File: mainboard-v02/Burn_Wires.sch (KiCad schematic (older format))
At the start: 41 parts, among them Q2 2N5088, Q3 2N5088, Q4 IRLML2803, Q5 IRLML2803, Q6 IRLML2803, Q7 IRLML2803, Q8 IRLML2803, U16 PE014006, U17 PE014006, U18 NDS8434, U19 NDS8434, U20 NDS8434, U21 NDS8434, U22 NDS8434

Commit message: fixing bold font and adding schematic pdf of v02
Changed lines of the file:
@@
 EESchema Schematic File Version 4
-LIBS:mainboard
 EELAYER 29 0
 EELAYER END
@@
 	6000 1700 6300 1700
 Connection ~ 6000 1700
-Text GLabel 6000 1700 0    10   BiDi ~ 0
+Text GLabel 6000 1700 0    10   BiDi ~ 2
 GND
 Wire Wire Line
@@
 	6000 2650 6000 2750
 Connection ~ 6000 2650
-Text GLabel 6300 2650 0    10   BiDi ~ 0
+Text GLabel 6300 2650 0    10   BiDi ~ 2
 GND
 Wire Wire Line
 	6400 4300 6100 4300
 Connection ~ 6100 4300
-Text GLabel 6400 4300 0    10   BiDi ~ 0
+Text GLabel 6400 4300 0    10   BiDi ~ 2
 GND
 Wire Wire Line
 	6100 5150 6400 5150
 Connection ~ 6100 5150
-Text GLabel 6100 5150 0    10   BiDi ~ 0
+Text GLabel 6100 5150 0    10   BiDi ~ 2
 GND
 Wire Wire Line
 	6100 6000 6400 6000
 Connection ~ 6100 6000
-Text GLabel 6100 6000 0    10   BiDi ~ 0
+Text GLabel 6100 6000 0    10   BiDi ~ 2
 GND
 Wire Wire Line
 	8600 2350 8900 2350
-Text GLabel 8600 2350 0    10   BiDi ~ 0
+Text GLabel 8600 2350 0    10   BiDi ~ 2
 GND
 Wire Wire Line
 	8700 4000 9000 4000
-Text GLabel 8700 4000 0    10   BiDi ~ 0
+Text GLabel 8700 4000 0    10   BiDi ~ 2
 GND
 Wire Wire Line
@@
 Wire Wire Line
 	5400 7400 5400 7500
-Text GLabel 5300 7400 0    10   BiDi ~ 0
+Text GLabel 5300 7400 0    10   BiDi ~ 2
 GND
 Wire Wire Line
@@
 Wire Wire Line
 	2000 7400 1900 7400
-Text GLabel 2000 7500 0    10   BiDi ~ 0
+Text GLabel 2000 7500 0    10   BiDi ~ 2
 GND
 Wire Wire Line
@@
 Wire Wire Line
 	3600 7400 3600 7500
-Text GLabel 3500 7400 0    10   BiDi ~ 0
+Text GLabel 3500 7400 0    10   BiDi ~ 2
 GND
 Wire Wire Line
 	8600 1400 8900 1400
-Text GLabel 8600 1400 0    10   BiDi ~ 0
+Text GLabel 8600 1400 0    10   BiDi ~ 2
 GND
 Wire Wire Line
 	8700 4850 9000 4850
-Text GLabel 8700 4850 0    10   BiDi ~ 0
+Text GLabel 8700 4850 0    10   BiDi ~ 2
 GND
 Wire Wire Line
 	8700 5700 9000 5700
-Text GLabel 8700 5700 0    10   BiDi ~ 0
+Text GLabel 8700 5700 0    10   BiDi ~ 2
 GND
 Wire Wire Line
@@
 	2000 2100 2300 2100
 Connection ~ 2300 2100
-Text GLabel 2300 2200 0    10   BiDi ~ 0
+Text GLabel 2300 2200 0    10   BiDi ~ 2
 GND
 Wire Wire Line
@@
 	2400 4500 2400 4700
 Connection ~ 2400 4700
-Text GLabel 2100 4700 0    10   BiDi ~ 0
+Text GLabel 2100 4700 0    10   BiDi ~ 2
 GND
 Text Label 8500 4000 2    50   ~ 0
@@
 	0    -1   -1   0
 $EndComp
-Text Notes 2700 1900 0    85   ~ 0
+Text Notes 2700 1900 0    85   ~ 17
 Power Relay A
-Text Notes 4500 800  0    85   ~ 0
+Text Notes 4500 800  0    85   ~ 17
 Burn Wire Control (Antenna Depolyment)
-Text Notes 4500 3300 0    85   ~ 0
+Text Notes 4500 3300 0    85   ~ 17
 Burn Wire Control (Sprite deployment)
-Text Notes 2800 4600 0    85   ~ 0
+Text Notes 2800 4600 0    85   ~ 17
 Power Relay B
-Text Notes 8200 1150 0    85   ~ 0
+Text Notes 8200 1150 0    85   ~ 17
 Antenna Board\nConnectors
-Text Notes 8300 3800 0    85   ~ 0
+Text Notes 8300 3800 0    85   ~ 17
 Solar Panel Board\nConnectors
-Text Notes 3000 6700 0    85   ~ 0
+Text Notes 3000 6700 0    85   ~ 17
 Solar Panel Connectors
 Wire Wire Line

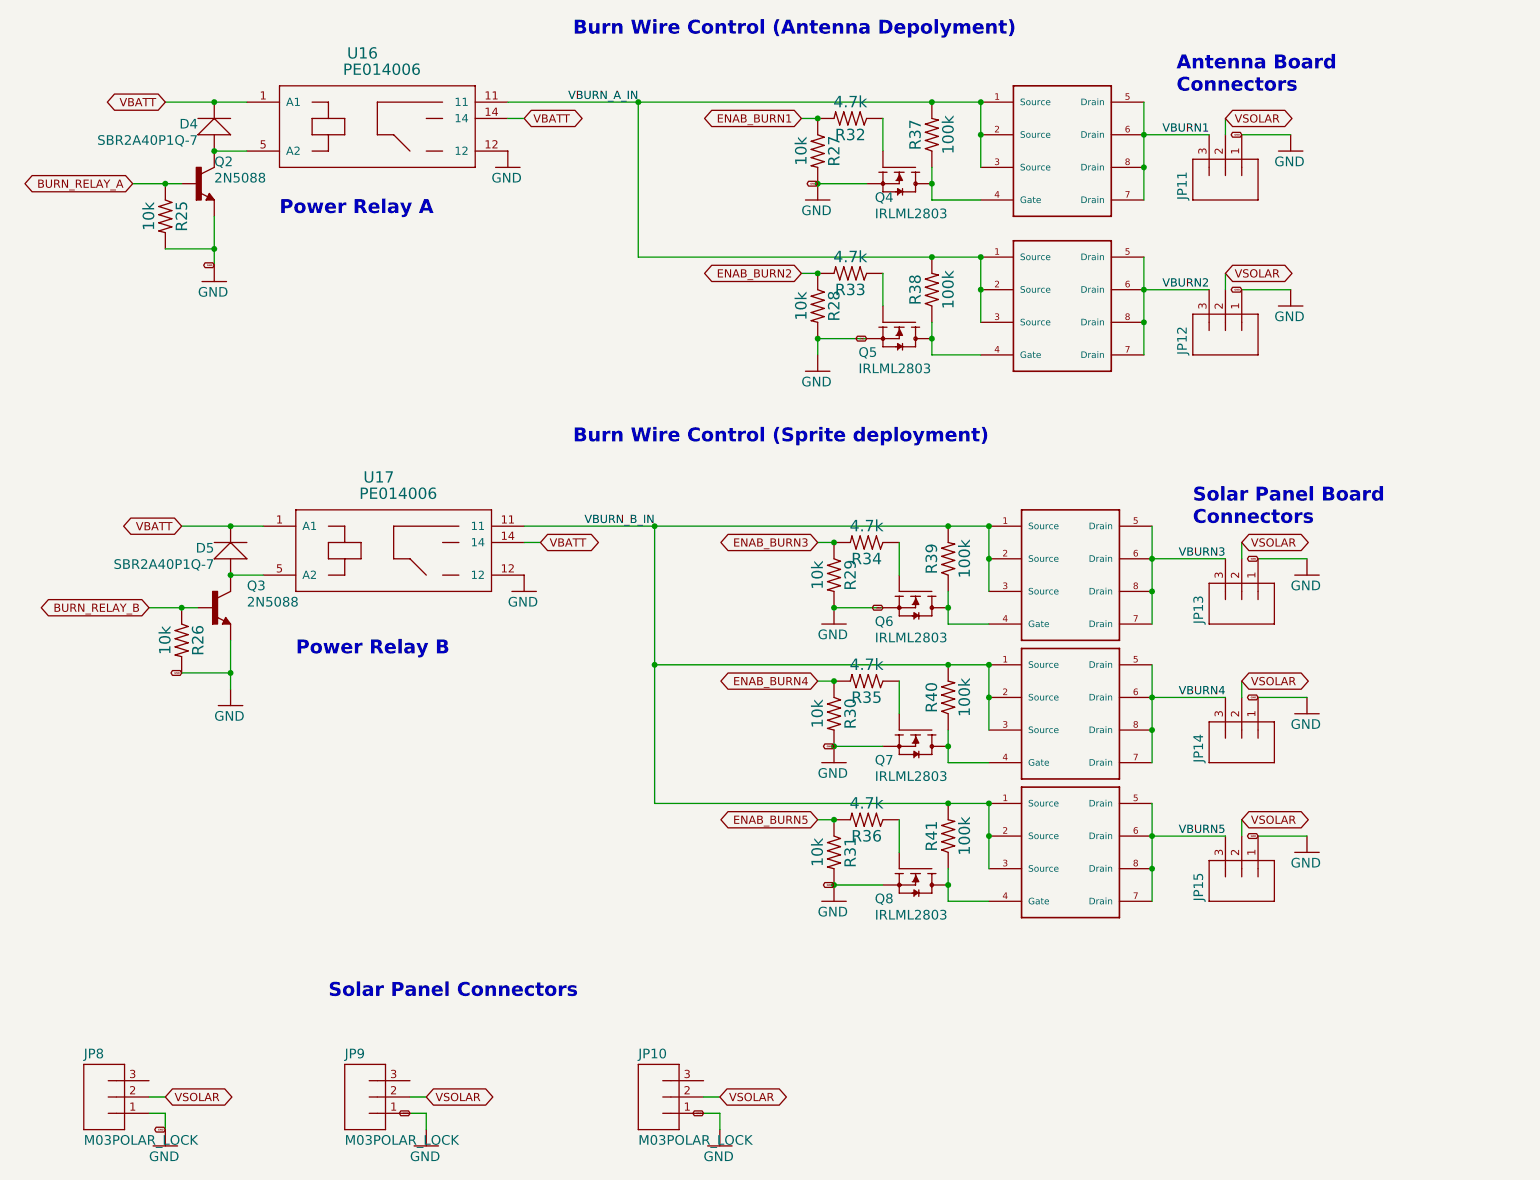
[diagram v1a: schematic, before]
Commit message: mainboard-v02 with RFM98PW
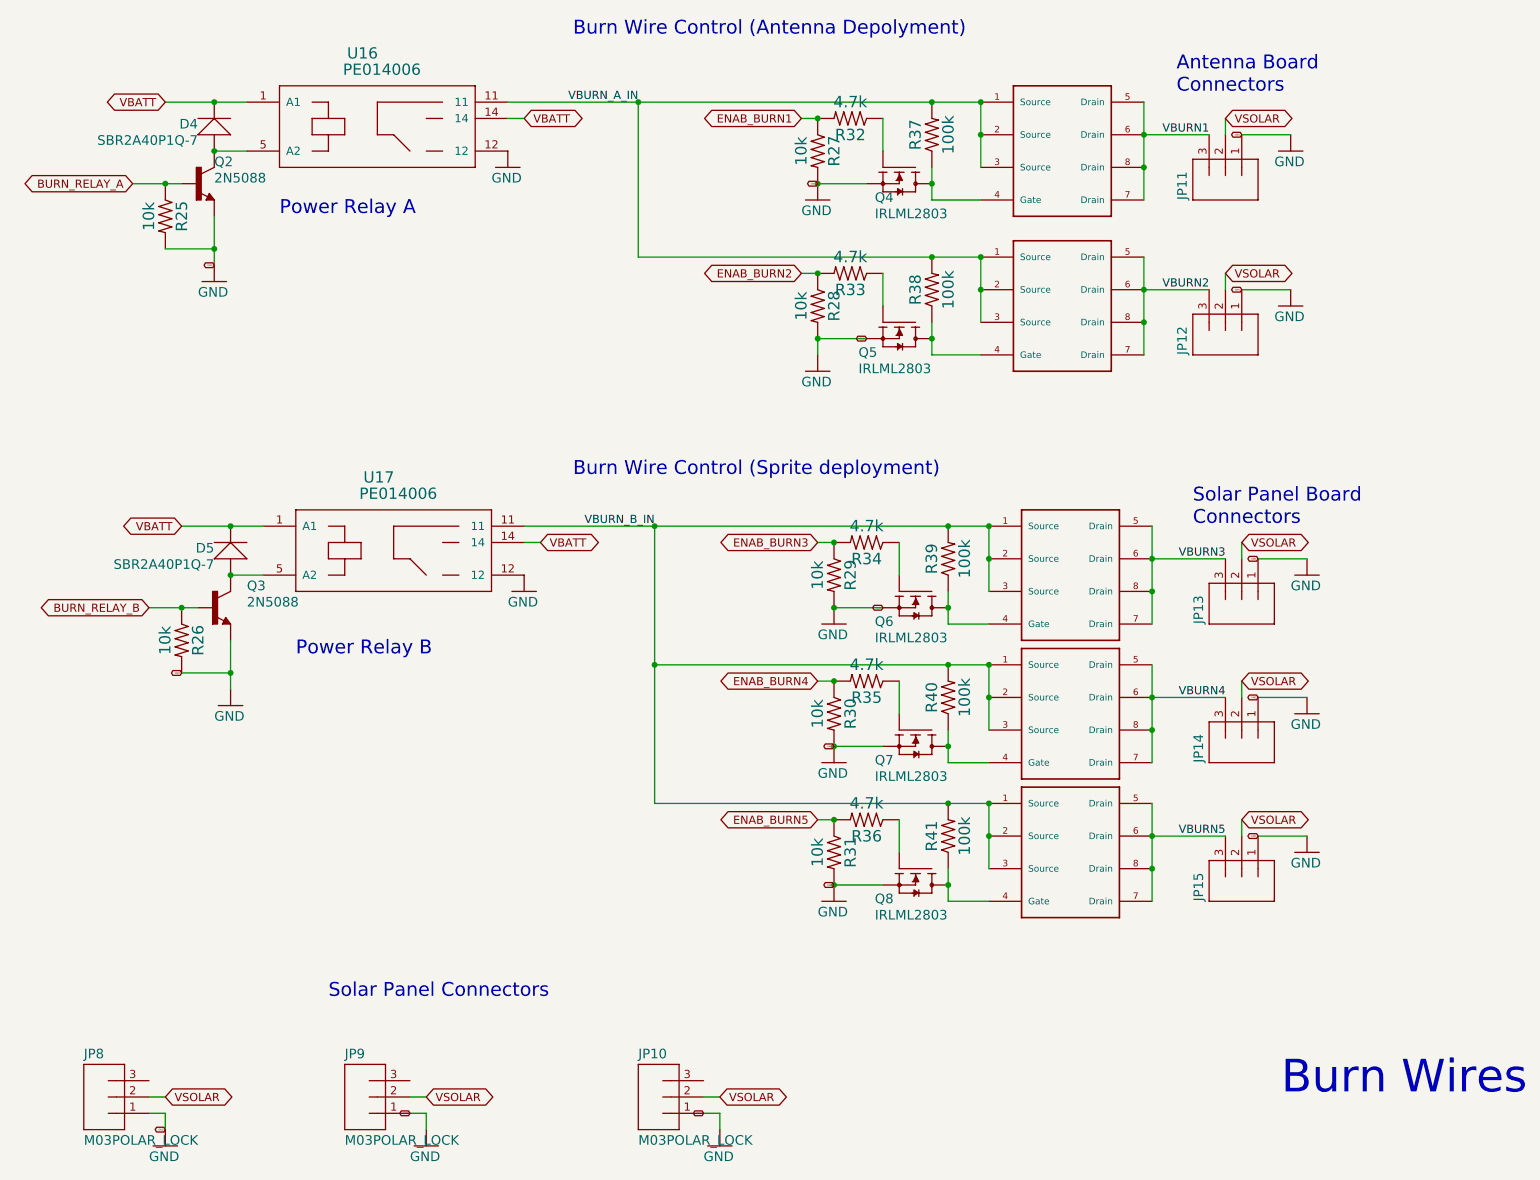
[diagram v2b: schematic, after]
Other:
- note added: "Burn Wires"
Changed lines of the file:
@@
 EESchema Schematic File Version 4
+LIBS:mainboard-cache
 EELAYER 29 0
 EELAYER END
@@
 	6000 1700 6300 1700
 Connection ~ 6000 1700
-Text GLabel 6000 1700 0    10   BiDi ~ 2
+Text GLabel 6000 1700 0    10   BiDi ~ 0
 GND
 Wire Wire Line
@@
 	6000 2650 6000 2750
 Connection ~ 6000 2650
-Text GLabel 6300 2650 0    10   BiDi ~ 2
+Text GLabel 6300 2650 0    10   BiDi ~ 0
 GND
 Wire Wire Line
 	6400 4300 6100 4300
 Connection ~ 6100 4300
-Text GLabel 6400 4300 0    10   BiDi ~ 2
+Text GLabel 6400 4300 0    10   BiDi ~ 0
 GND
 Wire Wire Line
 	6100 5150 6400 5150
 Connection ~ 6100 5150
-Text GLabel 6100 5150 0    10   BiDi ~ 2
+Text GLabel 6100 5150 0    10   BiDi ~ 0
 GND
 Wire Wire Line
 	6100 6000 6400 6000
 Connection ~ 6100 6000
-Text GLabel 6100 6000 0    10   BiDi ~ 2
+Text GLabel 6100 6000 0    10   BiDi ~ 0
 GND
 Wire Wire Line
 	8600 2350 8900 2350
-Text GLabel 8600 2350 0    10   BiDi ~ 2
+Text GLabel 8600 2350 0    10   BiDi ~ 0
 GND
 Wire Wire Line
 	8700 4000 9000 4000
-Text GLabel 8700 4000 0    10   BiDi ~ 2
+Text GLabel 8700 4000 0    10   BiDi ~ 0
 GND
 Wire Wire Line
@@
 Wire Wire Line
 	5400 7400 5400 7500
-Text GLabel 5300 7400 0    10   BiDi ~ 2
+Text GLabel 5300 7400 0    10   BiDi ~ 0
 GND
 Wire Wire Line
@@
 Wire Wire Line
 	2000 7400 1900 7400
-Text GLabel 2000 7500 0    10   BiDi ~ 2
+Text GLabel 2000 7500 0    10   BiDi ~ 0
 GND
 Wire Wire Line
@@
 Wire Wire Line
 	3600 7400 3600 7500
-Text GLabel 3500 7400 0    10   BiDi ~ 2
+Text GLabel 3500 7400 0    10   BiDi ~ 0
 GND
 Wire Wire Line
 	8600 1400 8900 1400
-Text GLabel 8600 1400 0    10   BiDi ~ 2
+Text GLabel 8600 1400 0    10   BiDi ~ 0
 GND
 Wire Wire Line
 	8700 4850 9000 4850
-Text GLabel 8700 4850 0    10   BiDi ~ 2
+Text GLabel 8700 4850 0    10   BiDi ~ 0
 GND
 Wire Wire Line
 	8700 5700 9000 5700
-Text GLabel 8700 5700 0    10   BiDi ~ 2
+Text GLabel 8700 5700 0    10   BiDi ~ 0
 GND
 Wire Wire Line
@@
 	2000 2100 2300 2100
 Connection ~ 2300 2100
-Text GLabel 2300 2200 0    10   BiDi ~ 2
+Text GLabel 2300 2200 0    10   BiDi ~ 0
 GND
 Wire Wire Line
@@
 	2400 4500 2400 4700
 Connection ~ 2400 4700
-Text GLabel 2100 4700 0    10   BiDi ~ 2
+Text GLabel 2100 4700 0    10   BiDi ~ 0
 GND
 Text Label 8500 4000 2    50   ~ 0
@@
 	0    -1   -1   0
 $EndComp
-Text Notes 2700 1900 0    85   ~ 17
+Text Notes 2700 1900 0    85   ~ 0
 Power Relay A
-Text Notes 4500 800  0    85   ~ 17
+Text Notes 4500 800  0    85   ~ 0
 Burn Wire Control (Antenna Depolyment)
-Text Notes 4500 3300 0    85   ~ 17
+Text Notes 4500 3500 0    85   ~ 0
 Burn Wire Control (Sprite deployment)
-Text Notes 2800 4600 0    85   ~ 17
+Text Notes 2800 4600 0    85   ~ 0
 Power Relay B
-Text Notes 8200 1150 0    85   ~ 17
+Text Notes 8200 1150 0    85   ~ 0
 Antenna Board\nConnectors
-Text Notes 8300 3800 0    85   ~ 17
+Text Notes 8300 3800 0    85   ~ 0
 Solar Panel Board\nConnectors
-Text Notes 3000 6700 0    85   ~ 17
+Text Notes 3000 6700 0    85   ~ 0
 Solar Panel Connectors
 Wire Wire Line
@@
 Wire Wire Line
 	5000 3800 5000 4650
+Text Notes 10350 7300 2    200  ~ 0
+Burn Wires
 $EndSCHEMATC
